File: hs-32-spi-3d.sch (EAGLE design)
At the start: 24 parts, among them U1 RHD2132_QFN, U2 BNO055, U3 TLV70725

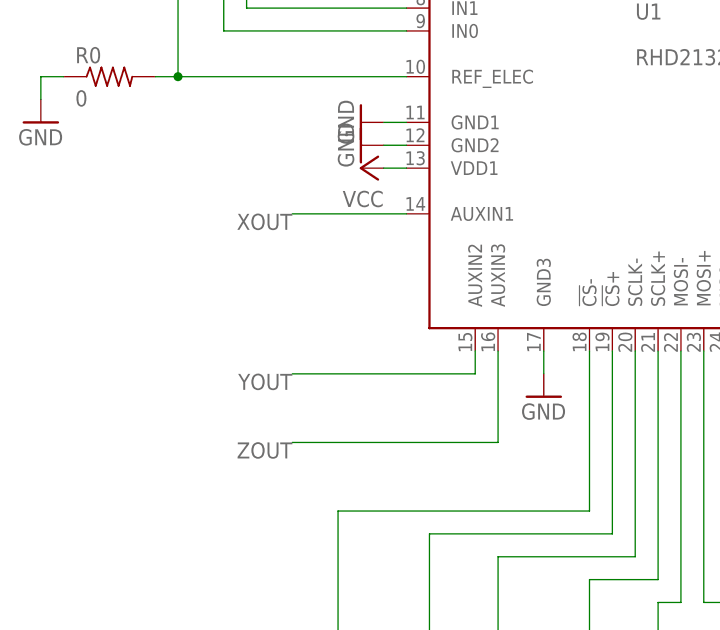
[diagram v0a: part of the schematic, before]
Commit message: Increased minimum drill to 0.25 mm.
Also created a pad for the AUXIN3.
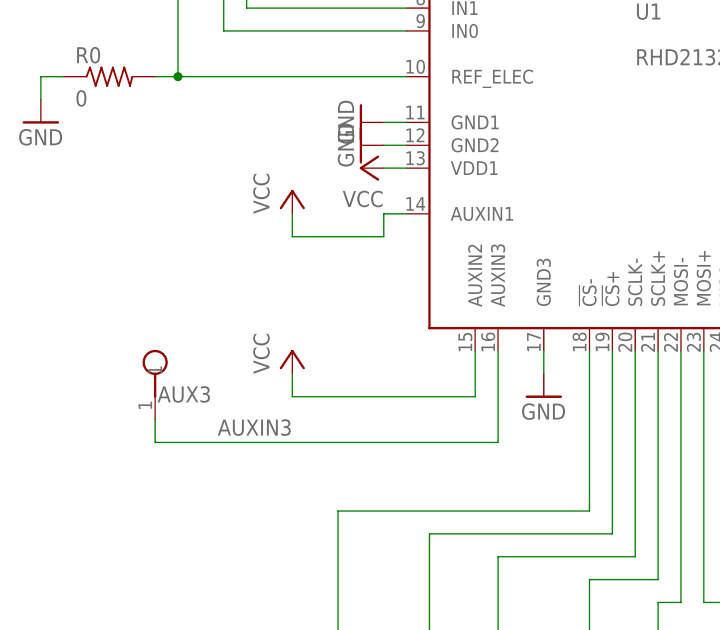
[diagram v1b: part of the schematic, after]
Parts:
- added AUX3: TESTPOINT_SMALL, RHD2000_eval_board:TESTPOINT_SMALL
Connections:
- removed net XOUT: U1.AUXIN1
- removed net YOUT: U1.AUXIN2
- removed net ZOUT: U1.AUXIN3
- new net AUXIN3: AUX3.1, U1.AUXIN3
- net VCC: now also U1.AUXIN1, U1.AUXIN2
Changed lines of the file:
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@@
 <part name="U$4" library="jonnew" deviceset="+2V5" device=""/>
 <part name="FRAME2" library="frames" library_urn="urn:adsk.eagle:library:229" deviceset="A3L-LOC" device=""/>
+<part name="P+9" library="supply1" deviceset="VCC" device=""/>
+<part name="P+11" library="supply1" deviceset="VCC" device=""/>
+<part name="AUX3" library="RHD2000_eval_board" deviceset="TESTPOINT" device="_SMALL"/>
 </parts>
 <sheets>
@@
 <attribute name="LAST_DATE_TIME" x="344.17" y="10.16" size="2.286" layer="94"/>
 <attribute name="SHEET" x="357.505" y="5.08" size="2.54" layer="94"/>
+</instance>
+<instance part="P+9" gate="VCC" x="55.88" y="132.08" smashed="yes">
+<attribute name="VALUE" x="53.34" y="129.54" size="1.778" layer="96" rot="R90"/>
+</instance>
+<instance part="P+11" gate="VCC" x="55.88" y="149.86" smashed="yes">
+<attribute name="VALUE" x="53.34" y="147.32" size="1.778" layer="96" rot="R90"/>
+</instance>
+<instance part="AUX3" gate="TP$1" x="40.64" y="132.08" smashed="yes">
+<attribute name="NAME" x="40.894" y="126.365" size="1.778" layer="95"/>
 </instance>
 </instances>
@@
 <pinref part="P+8" gate="VCC" pin="VCC"/>
 </segment>
+<segment>
+<pinref part="U1" gate="A" pin="AUXIN2"/>
+<wire x1="76.2" y1="132.08" x2="76.2" y2="127" width="0.1524" layer="91"/>
+<wire x1="76.2" y1="127" x2="55.88" y2="127" width="0.1524" layer="91"/>
+<wire x1="55.88" y1="127" x2="55.88" y2="129.54" width="0.1524" layer="91"/>
+<pinref part="P+9" gate="VCC" pin="VCC"/>
+</segment>
+<segment>
+<pinref part="U1" gate="A" pin="AUXIN1"/>
+<wire x1="55.88" y1="147.32" x2="55.88" y2="144.78" width="0.1524" layer="91"/>
+<wire x1="55.88" y1="144.78" x2="66.04" y2="144.78" width="0.1524" layer="91"/>
+<wire x1="66.04" y1="144.78" x2="66.04" y2="147.32" width="0.1524" layer="91"/>
+<wire x1="66.04" y1="147.32" x2="68.58" y2="147.32" width="0.1524" layer="91"/>
+<pinref part="P+11" gate="VCC" pin="VCC"/>
+</segment>
 </net>
 <net name="N$11" class="0">
@@
 </segment>
 </net>
-<net name="XOUT" class="0">
-<segment>
-<pinref part="U1" gate="A" pin="AUXIN1"/>
-<wire x1="55.88" y1="147.32" x2="68.58" y2="147.32" width="0.1524" layer="91"/>
-<label x="55.88" y="147.32" size="1.778" layer="95" rot="R180"/>
-</segment>
-</net>
-<net name="YOUT" class="0">
-<segment>
-<pinref part="U1" gate="A" pin="AUXIN2"/>
-<wire x1="76.2" y1="132.08" x2="76.2" y2="129.54" width="0.1524" layer="91"/>
-<wire x1="76.2" y1="129.54" x2="55.88" y2="129.54" width="0.1524" layer="91"/>
-<label x="55.88" y="129.54" size="1.778" layer="95" rot="R180"/>
-</segment>
-</net>
-<net name="ZOUT" class="0">
+<net name="AUXIN3" class="0">
 <segment>
 <pinref part="U1" gate="A" pin="AUXIN3"/>
-<wire x1="55.88" y1="121.92" x2="78.74" y2="121.92" width="0.1524" layer="91"/>
+<wire x1="40.64" y1="121.92" x2="78.74" y2="121.92" width="0.1524" layer="91"/>
 <wire x1="78.74" y1="121.92" x2="78.74" y2="132.08" width="0.1524" layer="91"/>
-<label x="55.88" y="121.92" size="1.778" layer="95" rot="R180"/>
-</segment>
-</net>
+<label x="55.88" y="124.46" size="1.778" layer="95" rot="R180"/>
+<pinref part="AUX3" gate="TP$1" pin="1"/>
+<wire x1="40.64" y1="121.92" x2="40.64" y2="124.46" width="0.1524" layer="91"/>
+</segment>
+</net>

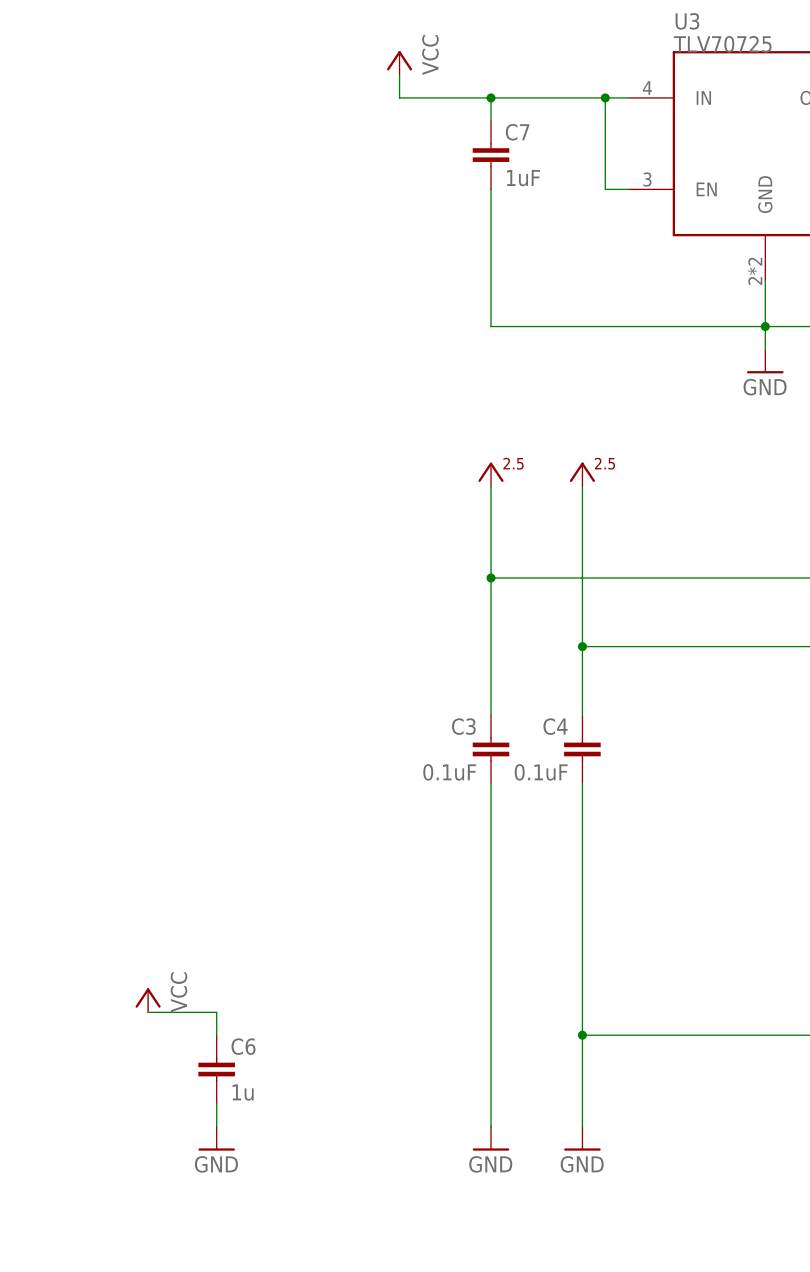
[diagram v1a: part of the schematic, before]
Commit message: Corrected C6 and C7 values to 4.7uF.
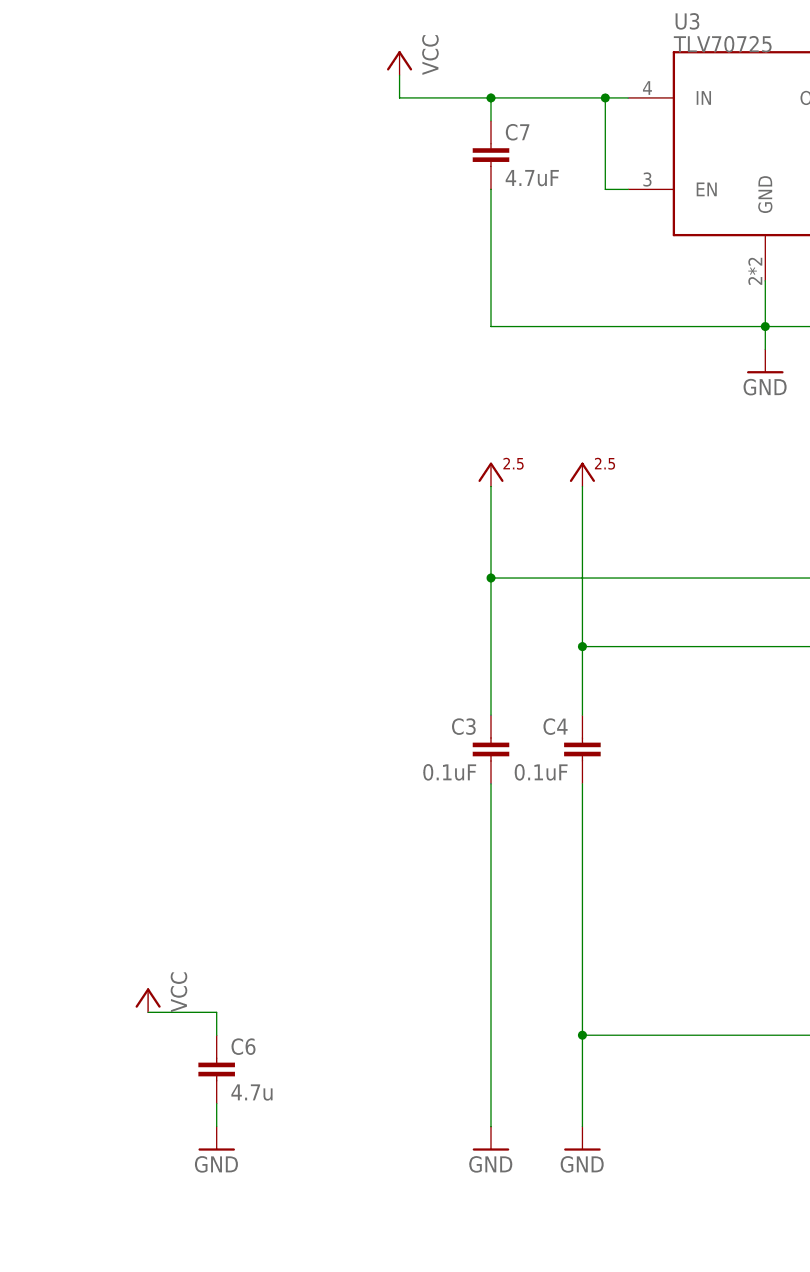
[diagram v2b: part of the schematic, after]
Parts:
- C6: value 1u -> 4.7u
- C7: value 1uF -> 4.7uF
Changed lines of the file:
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@@
 <part name="GND10" library="supply1" deviceset="GND" device=""/>
 <part name="REF" library="RHD2000_eval_board" deviceset="TESTPOINT" device="_SMALL"/>
-<part name="C6" library="jonnew" deviceset="C" device="_0402" value="1u"/>
+<part name="C6" library="jonnew" deviceset="C" device="_0402" value="4.7u"/>
 <part name="C4" library="jonnew" deviceset="C" device="_0402T" value="0.1uF"/>
 <part name="C3" library="jonnew" deviceset="C" device="_0402T" value="0.1uF"/>
@@
 <part name="U3" library="jonnew" deviceset="TLV707" device="" value="TLV70725"/>
 <part name="U$45" library="jonnew" deviceset="+2V5" device=""/>
-<part name="C7" library="jonnew" deviceset="C" device="_0402T" value="1uF">
+<part name="C7" library="jonnew" deviceset="C" device="_0402T" value="4.7uF">
 <attribute name="PARTNO" value="CL05A105KO5NNNC"/>
 </part>
